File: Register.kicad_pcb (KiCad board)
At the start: 2 copper layers, 254 x 127.9 mm, 71 parts, among them U1 74LS173, U2 74LS173, U3 74LS173, U4 74LS173, U5 74LS173, U6 74LS173, U7 74LS173, U8 74LS173

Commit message: Added footprints
Added footprints for 74LS245s (SOIC 20, 12.8x7.5mm, 1.27mm pitch)
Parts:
- added U10: 74LS245, Package_SO:SOIC-20W_7.5x12.8mm_P1.27mm, F.Cu at (76.2, 78.1)
- added U11: 74LS245, Package_SO:SOIC-20W_7.5x12.8mm_P1.27mm, F.Cu at (89.1, 78.1)
- added U12: 74LS245, Package_SO:SOIC-20W_7.5x12.8mm_P1.27mm, F.Cu at (102.0, 78.1)
- added U9: 74LS245, Package_SO:SOIC-20W_7.5x12.8mm_P1.27mm, F.Cu at (63.3, 78.1)
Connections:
- U1 pad 3: /Q1 -> Net-(U1-Q0)
- U1 pad 4: /Q2 -> Net-(U1-Q1)
- U1 pad 5: /Q3 -> Net-(U1-Q2)
- U1 pad 6: /Q4 -> Net-(U1-Q3)
- U2 pad 3: /Q5 -> Net-(U2-Q0)
- U2 pad 4: /Q6 -> Net-(U2-Q1)
- U2 pad 5: /Q7 -> Net-(U2-Q2)
- U2 pad 6: /Q8 -> Net-(U2-Q3)
- U3 pad 1: Net-(U3-Oe1) -> unconnected-(U3-Oe1-Pad1)
- U3 pad 2: Net-(U3-Oe1) -> unconnected-(U3-Oe2-Pad2)
- U3 pad 3: /Q9 -> Net-(U10-A0)
- U3 pad 4: /Q10 -> Net-(U10-A1)
- U3 pad 5: /Q11 -> Net-(U10-A2)
- U3 pad 6: /Q12 -> Net-(U10-A3)
- U4 pad 3: /Q13 -> Net-(U10-A4)
- U4 pad 4: /Q14 -> Net-(U10-A5)
- U4 pad 5: /Q15 -> Net-(U10-A6)
- U4 pad 6: /Q16 -> Net-(U10-A7)
- U5 pad 3: /Q17 -> Net-(U11-A0)
- U5 pad 4: /Q18 -> Net-(U11-A1)
- U5 pad 5: /Q19 -> Net-(U11-A2)
- U5 pad 6: /Q20 -> Net-(U11-A3)
- U6 pad 3: /Q21 -> Net-(U11-A4)
- U6 pad 4: /Q22 -> Net-(U11-A5)
- U6 pad 5: /Q23 -> Net-(U11-A6)
- U6 pad 6: /Q24 -> Net-(U11-A7)
- U7 pad 3: /Q25 -> Net-(U12-A0)
- U7 pad 4: /Q26 -> Net-(U12-A1)
- U7 pad 5: /Q27 -> Net-(U12-A2)
- U7 pad 6: /Q28 -> Net-(U12-A3)
- U8 pad 3: /Q29 -> Net-(U12-A4)
- U8 pad 4: /Q30 -> Net-(U12-A5)
- U8 pad 5: /Q31 -> Net-(U12-A6)
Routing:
- net Net-(U3-Oe1): track 1.27 -> 0.00 mm
- net (no net): track 0.00 -> 1.27 mm

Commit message: Update PCB
Updated PCB with recent rewiring changes
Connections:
- U1 pad 11: /D4 -> /D3
- U1 pad 12: /D3 -> /D2
- U1 pad 13: /D2 -> /D1
- U1 pad 14: /D1 -> /D0
- U12 pad 11: GND -> unconnected-(U12-B7-Pad11)
- U12 pad 14: unconnected-(U12-B4-Pad14) -> GND
- U12 pad 6: Net-(U12-A4) -> GND
- U12 pad 9: GND -> Net-(U12-A7)
- U3 pad 3: Net-(U10-A0) -> Net-(U10-A3)
- U3 pad 4: Net-(U10-A1) -> Net-(U10-A2)
- U3 pad 5: Net-(U10-A2) -> Net-(U10-A1)
- U3 pad 6: Net-(U10-A3) -> Net-(U10-A0)
- U4 pad 3: Net-(U10-A4) -> Net-(U10-A7)
- U4 pad 4: Net-(U10-A5) -> Net-(U10-A6)
- U4 pad 5: Net-(U10-A6) -> Net-(U10-A5)
- U4 pad 6: Net-(U10-A7) -> Net-(U10-A4)
- U5 pad 3: Net-(U11-A0) -> Net-(U11-A3)
- U5 pad 4: Net-(U11-A1) -> Net-(U11-A2)
- U5 pad 5: Net-(U11-A2) -> Net-(U11-A1)
- U5 pad 6: Net-(U11-A3) -> Net-(U11-A0)
- U6 pad 3: Net-(U11-A4) -> Net-(U11-A7)
- U6 pad 4: Net-(U11-A5) -> Net-(U11-A6)
- U6 pad 5: Net-(U11-A6) -> Net-(U11-A5)
- U6 pad 6: Net-(U11-A7) -> Net-(U11-A4)
- U7 pad 3: Net-(U12-A0) -> Net-(U12-A3)
- U7 pad 4: Net-(U12-A1) -> Net-(U12-A2)
- U7 pad 5: Net-(U12-A2) -> Net-(U12-A1)
- U7 pad 6: Net-(U12-A3) -> Net-(U12-A0)
- U8 pad 3: Net-(U12-A4) -> Net-(U12-A7)
- U8 pad 4: Net-(U12-A5) -> Net-(U12-A6)
- U8 pad 5: Net-(U12-A6) -> Net-(U12-A5)
- U9 pad 2: Net-(U1-Q0) -> Net-(U1-Q3)
- U9 pad 3: Net-(U1-Q1) -> Net-(U1-Q2)
- U9 pad 4: Net-(U1-Q2) -> Net-(U1-Q1)
- U9 pad 5: Net-(U1-Q3) -> Net-(U1-Q0)
- U9 pad 6: Net-(U2-Q0) -> Net-(U2-Q3)
- U9 pad 7: Net-(U2-Q1) -> Net-(U2-Q2)
- U9 pad 8: Net-(U2-Q2) -> Net-(U2-Q1)
- U9 pad 9: Net-(U2-Q3) -> Net-(U2-Q0)

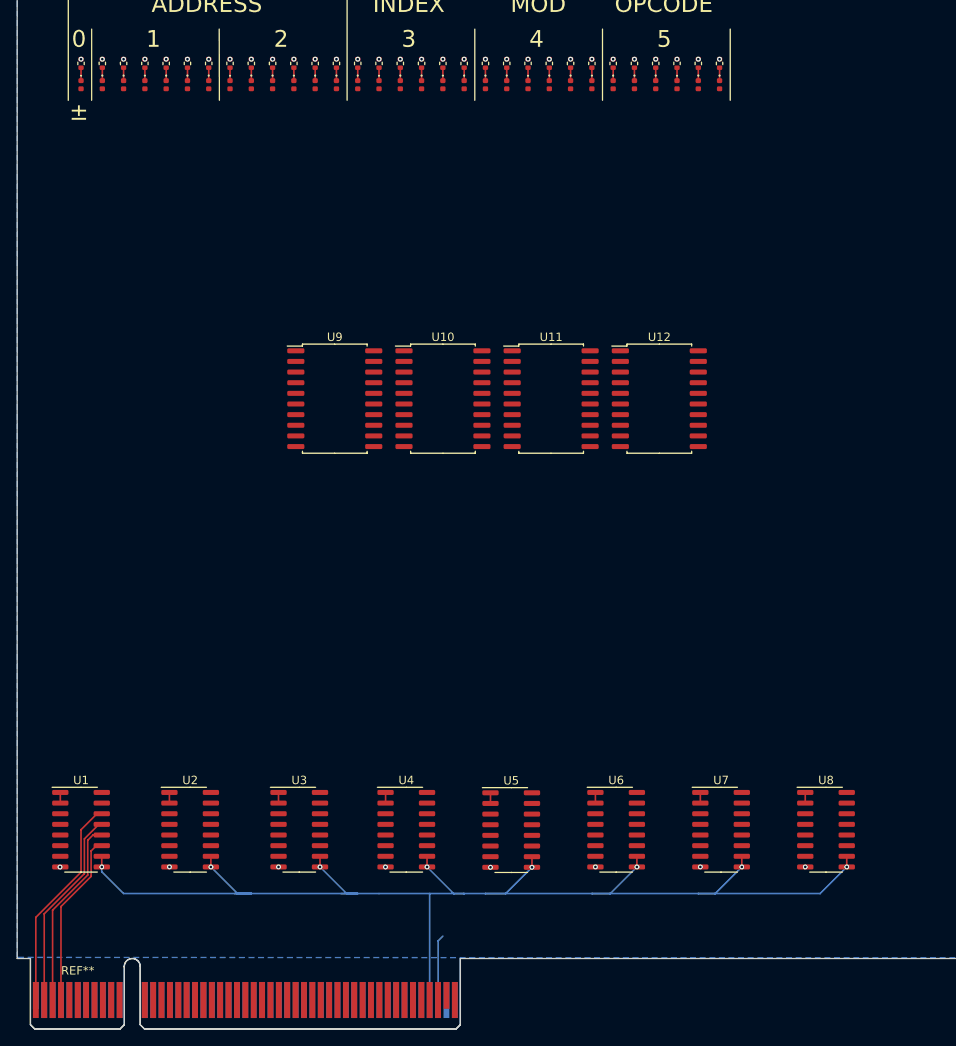
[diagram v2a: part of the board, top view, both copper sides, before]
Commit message: Rearranged registers and xcvrs
Moved registers and bus transceivers into position relative to one another.

Also moved LED grounding vias off of solder pads.
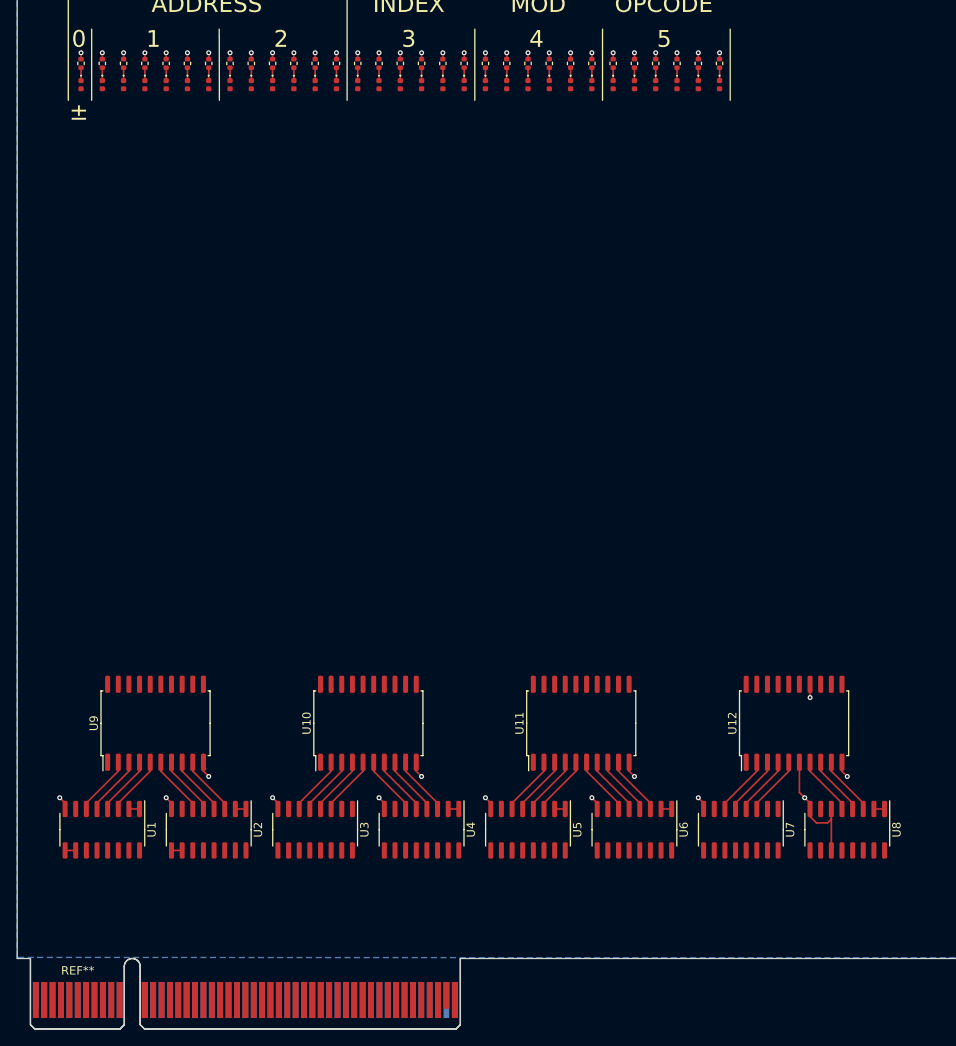
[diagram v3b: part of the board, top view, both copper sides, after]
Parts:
- moved U9 44.2 mm to (41.9, 116.8), turned to 90 degrees
- moved U12 41.9 mm to (118.1, 116.8), turned to 90 degrees
- moved U10 39.7 mm to (67.3, 116.8), turned to 90 degrees
- moved U11 38.9 mm to (92.7, 116.8), turned to 90 degrees
- moved U1 2.54 mm to (35.6, 129.5), turned to -90 degrees
- moved U8 2.54 mm to (124.5, 129.5), turned to -90 degrees
- moved U7 2.36 mm to (111.8, 129.5), turned to -90 degrees
- moved U2 2.22 mm to (48.3, 129.5), turned to -90 degrees
- moved U6 2.18 mm to (99.1, 129.5), turned to -90 degrees
- moved U5 2.00 mm to (86.4, 129.5), turned to -90 degrees
- moved U3 1.90 mm to (61.0, 129.5), turned to -90 degrees
- moved U4 1.83 mm to (73.7, 129.5), turned to -90 degrees
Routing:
- net /DR: track 156.4 -> 2.54 mm, vias 8 -> 0
- net GND: track 7.86 -> 59.2 mm, vias 39 -> 44
- net /D1: track 26.0 -> 0.00 mm
- net /D2: track 24.1 -> 0.00 mm
- net /D3: track 22.9 -> 0.00 mm
- net /D4: track 20.9 -> 0.00 mm
- net Net-(U2-Q2): track 0.00 -> 7.15 mm
- net Net-(U2-Q1): track 0.00 -> 7.15 mm
- net Net-(U2-Q0): track 0.00 -> 7.15 mm
- net Net-(U12-A6): track 0.00 -> 7.15 mm
- net Net-(U12-A5): track 0.00 -> 7.15 mm
- net Net-(U12-A2): track 0.00 -> 7.15 mm
- net Net-(U12-A1): track 0.00 -> 7.15 mm
- net Net-(U12-A0): track 0.00 -> 7.15 mm
- net Net-(U11-A7): track 0.00 -> 7.15 mm
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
